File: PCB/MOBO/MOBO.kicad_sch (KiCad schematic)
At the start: 6 parts, among them J103 RPi_GPio, J104 RPi_GND, J105 RPi_5V, J106 RPi_DM, J107 RPi_DM, J7 RPi_TV

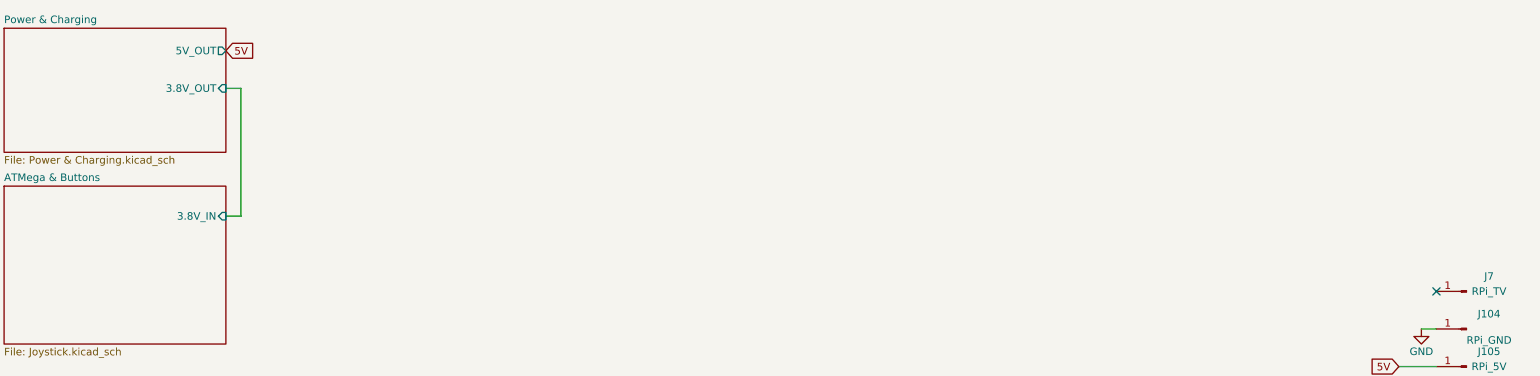
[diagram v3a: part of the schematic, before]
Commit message: fixed sheet conections and added wiring
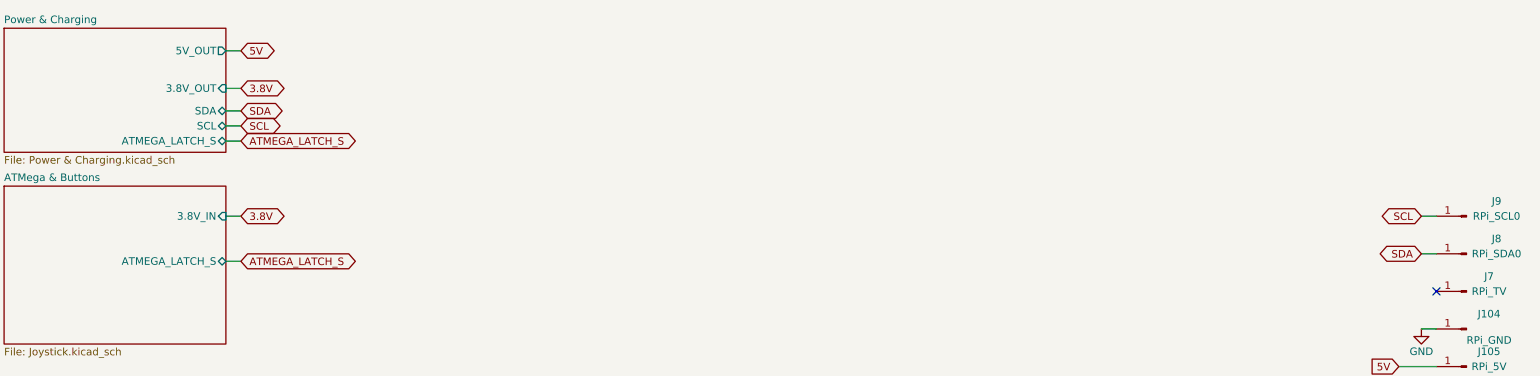
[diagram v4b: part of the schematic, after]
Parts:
- added J8: RPi_SDA0, TestPoint:TestPoint_Pad_1.5x1.5mm, symbol Connector:Conn_01x01_Male
- added J9: RPi_SCL0, TestPoint:TestPoint_Pad_1.5x1.5mm, symbol Connector:Conn_01x01_Male
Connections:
- new net SCL: J9.1 (Pin_1)
- new net SDA: J8.1 (Pin_1)
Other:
- sheet ATMega & Buttons ports: added ATMEGA_LATCH_S; removed none
- sheet Power & Charging ports: added ATMEGA_LATCH_S, SCL, SDA; removed none
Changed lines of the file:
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@@
   (no_connect (at 273.05 148.59))
   (no_connect (at 273.05 102.87))
+  (wire (pts (xy 264.16 57.15) (xy 261.62 57.15))
+    (stroke (width 0) (type default))
+  )
   (wire (pts (xy 59.69 29.21) (xy 62.23 29.21))
     (stroke (width 0) (type default))
   )
-  (wire (pts (xy 62.23 50.8) (xy 59.69 50.8))
+  (wire (pts (xy 59.69 35.56) (xy 62.23 35.56))
+    (stroke (width 0) (type default))
+  )
+  (wire (pts (xy 264.16 50.8) (xy 261.62 50.8))
     (stroke (width 0) (type default))
   )
@@
     (stroke (width 0) (type default))
   )
-  (wire (pts (xy 62.23 29.21) (xy 62.23 50.8))
+  (wire (pts (xy 59.69 58.42) (xy 62.23 58.42))
+    (stroke (width 0) (type default))
+  )
+  (wire (pts (xy 59.69 38.1) (xy 62.23 38.1))
+    (stroke (width 0) (type default))
+  )
+  (wire (pts (xy 59.69 22.86) (xy 62.23 22.86))
+    (stroke (width 0) (type default))
+  )
+  (wire (pts (xy 59.69 50.8) (xy 62.23 50.8))
     (stroke (width 0) (type default))
   )
   (wire (pts (xy 257.81 76.2) (xy 264.16 76.2))
+    (stroke (width 0) (type default))
+  )
+  (wire (pts (xy 59.69 33.02) (xy 62.23 33.02))
     (stroke (width 0) (type default))
   )
@@
     (effects (font (size 1.27 1.27)) (justify left bottom))
   )
-  (global_label "5V" (shape input) (at 59.69 22.86 0) (fields_autoplaced)
-    (effects (font (size 1.27 1.27)) (justify left))
-    (property "Intersheetrefs" "${INTERSHEET_REFS}" (at 64.9733 22.86 0)
-      (effects (font (size 1.27 1.27)) (justify left) hide)
+  (global_label "ATMEGA_LATCH_S" (shape bidirectional) (at 62.23 38.1 0) (fields_autoplaced)
+    (effects (font (size 1.27 1.27)) (justify left))
+    (property "Intersheetrefs" "${INTERSHEET_REFS}" (at 82.1712 38.1 0)
+      (effects (font (size 1.27 1.27)) (justify left) hide)
+    )
+  )
+  (global_label "ATMEGA_LATCH_S" (shape bidirectional) (at 62.23 58.42 0) (fields_autoplaced)
+    (effects (font (size 1.27 1.27)) (justify left))
+    (property "Intersheetrefs" "${INTERSHEET_REFS}" (at 82.1712 58.42 0)
+      (effects (font (size 1.27 1.27)) (justify left) hide)
+    )
+  )
+  (global_label "SCL" (shape bidirectional) (at 261.62 50.8 180) (fields_autoplaced)
+    (effects (font (size 1.27 1.27)) (justify right))
+    (property "Intersheetrefs" "${INTERSHEET_REFS}" (at 254.0159 50.8 0)
+      (effects (font (size 1.27 1.27)) (justify right) hide)
+    )
+  )
+  (global_label "5V" (shape bidirectional) (at 62.23 22.86 0) (fields_autoplaced)
+    (effects (font (size 1.27 1.27)) (justify left))
+    (property "Intersheetrefs" "${INTERSHEET_REFS}" (at 68.6246 22.86 0)
+      (effects (font (size 1.27 1.27)) (justify left) hide)
+    )
+  )
+  (global_label "SDA" (shape bidirectional) (at 261.62 57.15 180) (fields_autoplaced)
+    (effects (font (size 1.27 1.27)) (justify right))
+    (property "Intersheetrefs" "${INTERSHEET_REFS}" (at 253.9554 57.15 0)
+      (effects (font (size 1.27 1.27)) (justify right) hide)
     )
   )
@@
     (property "Intersheetrefs" "${INTERSHEET_REFS}" (at 252.5267 76.2 0)
       (effects (font (size 1.27 1.27)) (justify right) hide)
+    )
+  )
+  (global_label "SCL" (shape bidirectional) (at 62.23 35.56 0) (fields_autoplaced)
+    (effects (font (size 1.27 1.27)) (justify left))
+    (property "Intersheetrefs" "${INTERSHEET_REFS}" (at 69.8341 35.56 0)
+      (effects (font (size 1.27 1.27)) (justify left) hide)
+    )
+  )
+  (global_label "3.8V" (shape bidirectional) (at 62.23 50.8 0) (fields_autoplaced)
+    (effects (font (size 1.27 1.27)) (justify left))
+    (property "Intersheetrefs" "${INTERSHEET_REFS}" (at 70.4389 50.8 0)
+      (effects (font (size 1.27 1.27)) (justify left) hide)
+    )
+  )
+  (global_label "3.8V" (shape bidirectional) (at 62.23 29.21 0) (fields_autoplaced)
+    (effects (font (size 1.27 1.27)) (justify left))
+    (property "Intersheetrefs" "${INTERSHEET_REFS}" (at 70.4389 29.21 0)
+      (effects (font (size 1.27 1.27)) (justify left) hide)
+    )
+  )
+  (global_label "SDA" (shape bidirectional) (at 62.23 33.02 0) (fields_autoplaced)
+    (effects (font (size 1.27 1.27)) (justify left))
+    (property "Intersheetrefs" "${INTERSHEET_REFS}" (at 69.8946 33.02 0)
+      (effects (font (size 1.27 1.27)) (justify left) hide)
+    )
+  )
+  (symbol (lib_id "Connector:Conn_01x01_Male") (at 269.24 50.8 180) (unit 1)
+    (in_bom yes) (on_board yes) (dnp no)
+    (property "Reference" "J9" (at 274.32 48.26 0)
+      (effects (font (size 1.27 1.27)))
+    )
+    (property "Value" "RPi_SCL0" (at 274.32 50.8 0)
+      (effects (font (size 1.27 1.27)))
+    )
+    (property "Footprint" "TestPoint:TestPoint_Pad_1.5x1.5mm" (at 269.24 50.8 0)
+      (effects (font (size 1.27 1.27)) hide)
+    )
+    (property "Datasheet" "~" (at 269.24 50.8 0)
+      (effects (font (size 1.27 1.27)) hide)
+    )
+    (pin "1")
+    (instances
+      (project "MOBO"
+        (path "/2d62a3c1-c4f2-4921-9f6b-8dc8aef69d64"
+          (reference "J9") (unit 1)
+        )
+      )
     )
   )
@@
     )
   )
+  (symbol (lib_id "Connector:Conn_01x01_Male") (at 269.24 57.15 180) (unit 1)
+    (in_bom yes) (on_board yes) (dnp no)
+    (property "Reference" "J8" (at 274.32 54.61 0)
+      (effects (font (size 1.27 1.27)))
+    )
+    (property "Value" "RPi_SDA0" (at 274.32 57.15 0)
+      (effects (font (size 1.27 1.27)))
+    )
+    (property "Footprint" "TestPoint:TestPoint_Pad_1.5x1.5mm" (at 269.24 57.15 0)
+      (effects (font (size 1.27 1.27)) hide)
+    )
+    (property "Datasheet" "~" (at 269.24 57.15 0)
+      (effects (font (size 1.27 1.27)) hide)
+    )
+    (pin "1")
+    (instances
+      (project "MOBO"
+        (path "/2d62a3c1-c4f2-4921-9f6b-8dc8aef69d64"
+          (reference "J8") (unit 1)
+        )
+      )
+    )
+  )
   (symbol (lib_id "power:GND") (at 261.62 69.85 0) (unit 1)
     (in_bom yes) (on_board yes) (dnp no)
@@
       (effects (font (size 1.27 1.27)) (justify right))
     )
+    (pin "ATMEGA_LATCH_S" bidirectional (at 59.69 58.42 0)
+      (effects (font (size 1.27 1.27)) (justify right))
+    )
     (instances
       (project "MOBO"
@@
       (effects (font (size 1.27 1.27)) (justify right))
     )
+    (pin "SDA" bidirectional (at 59.69 33.02 0)
+      (effects (font (size 1.27 1.27)) (justify right))
+    )
+    (pin "SCL" bidirectional (at 59.69 35.56 0)
+      (effects (font (size 1.27 1.27)) (justify right))
+    )
+    (pin "ATMEGA_LATCH_S" bidirectional (at 59.69 38.1 0)
+      (effects (font (size 1.27 1.27)) (justify right))
+    )

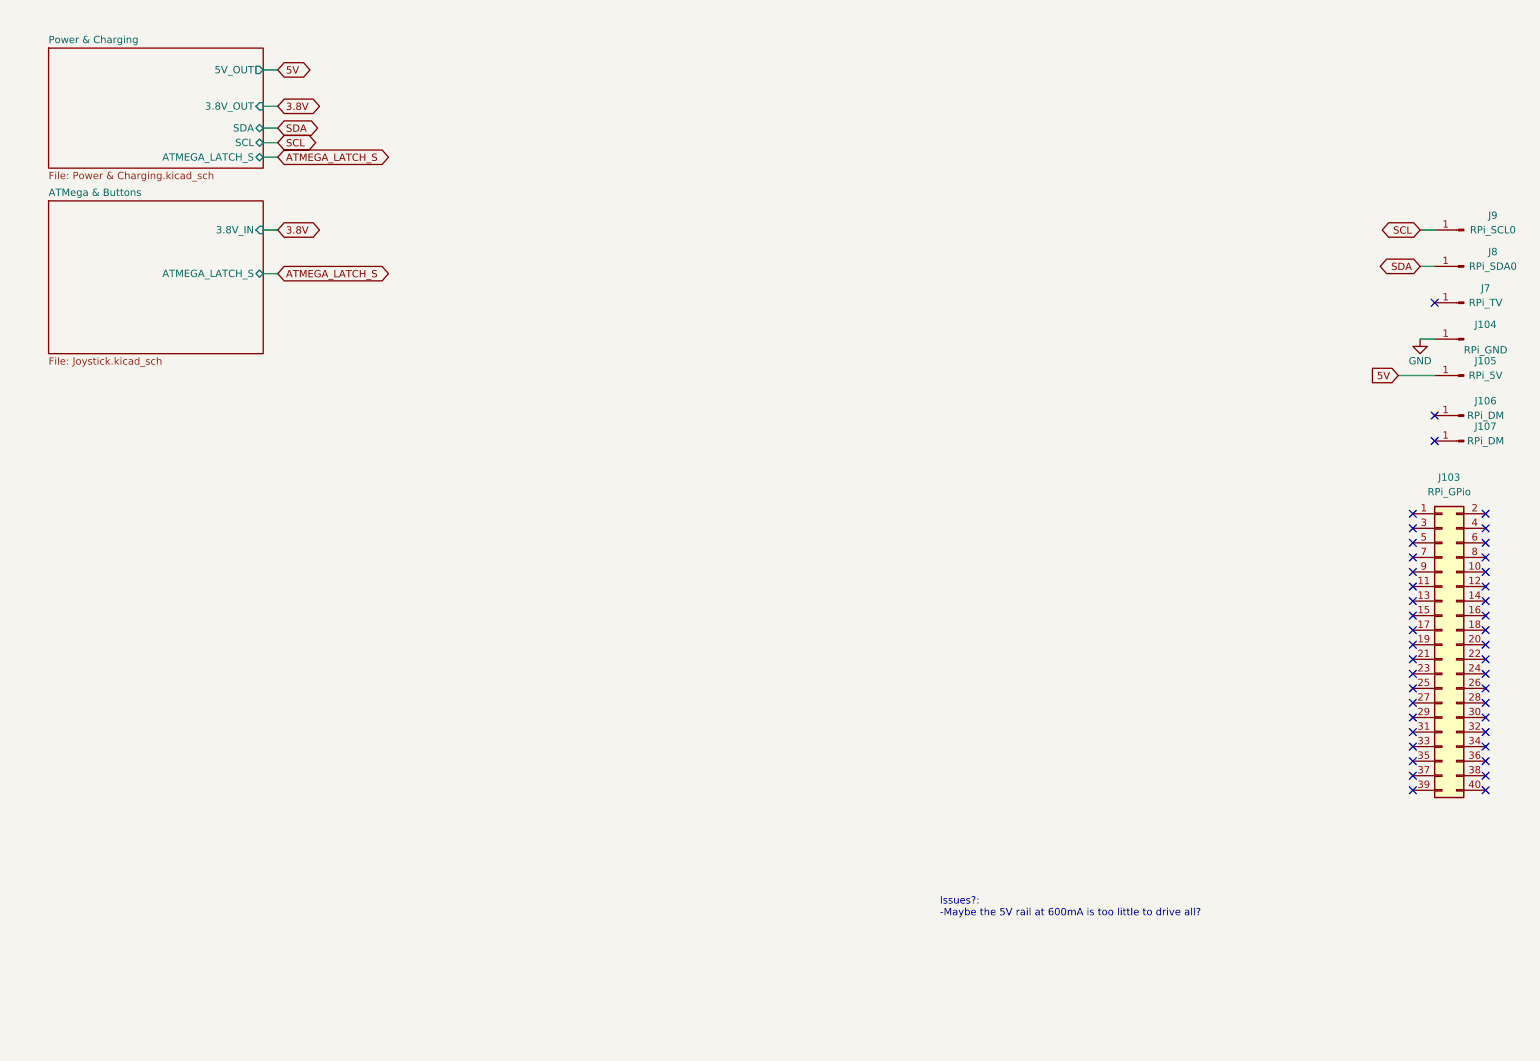
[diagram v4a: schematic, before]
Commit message: added 5V-GND-TV lines
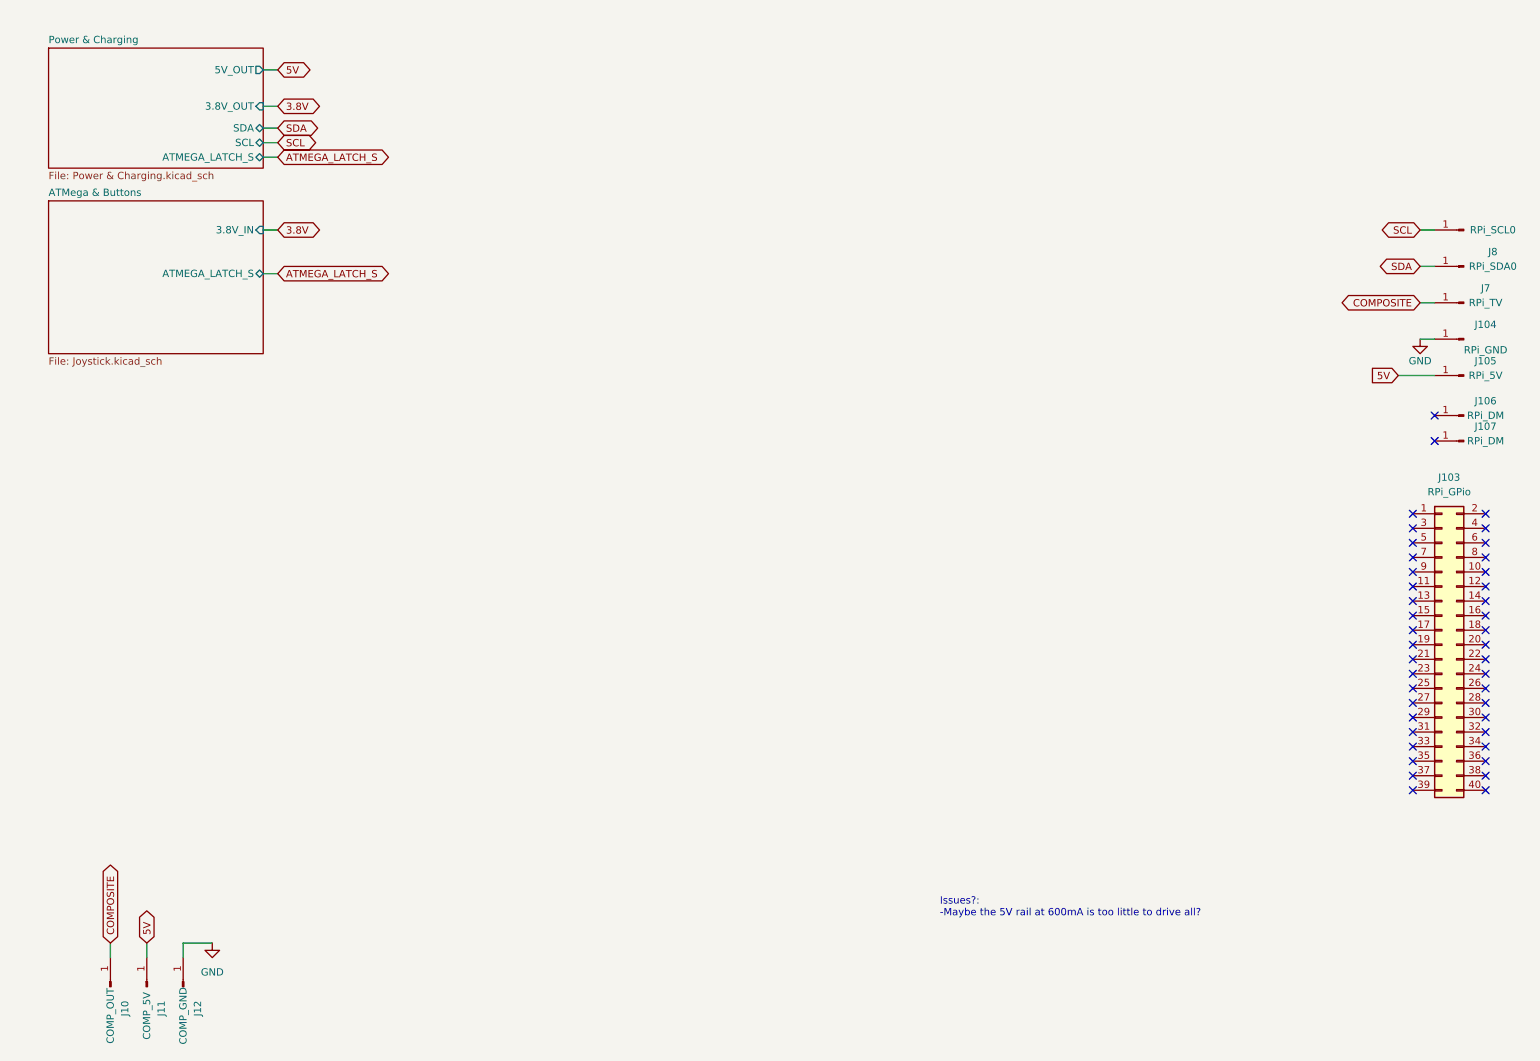
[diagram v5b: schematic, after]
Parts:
- added J10: COMP_OUT, TestPoint:TestPoint_Pad_1.5x1.5mm, symbol Connector:Conn_01x01_Male
- added J11: COMP_5V, TestPoint:TestPoint_Pad_1.5x1.5mm, symbol Connector:Conn_01x01_Male
- added J12: COMP_GND, TestPoint:TestPoint_Pad_1.5x1.5mm, symbol Connector:Conn_01x01_Male
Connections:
- net 5V: now also J11.1 (Pin_1)
- net GND: now also J12.1 (Pin_1)
- net COMPOSITE: now reaches J7.1 (Pin_1)
- net COMPOSITE: now also J10.1 (Pin_1)
- no-connect marks 43 -> 42
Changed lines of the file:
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@@
   (no_connect (at 273.05 120.65))
   (no_connect (at 260.35 102.87))
-  (no_connect (at 264.16 63.5))
   (no_connect (at 273.05 140.97))
   (no_connect (at 260.35 115.57))
@@
     (stroke (width 0) (type default))
   )
+  (wire (pts (xy 33.02 175.26) (xy 33.02 177.8))
+    (stroke (width 0) (type default))
+  )
   (wire (pts (xy 261.62 69.85) (xy 264.16 69.85))
     (stroke (width 0) (type default))
@@
     (stroke (width 0) (type default))
   )
+  (wire (pts (xy 45.72 175.26) (xy 50.8 175.26))
+    (stroke (width 0) (type default))
+  )
+  (wire (pts (xy 39.37 175.26) (xy 39.37 177.8))
+    (stroke (width 0) (type default))
+  )
   (wire (pts (xy 59.69 22.86) (xy 62.23 22.86))
+    (stroke (width 0) (type default))
+  )
+  (wire (pts (xy 45.72 175.26) (xy 45.72 177.8))
+    (stroke (width 0) (type default))
+  )
+  (wire (pts (xy 261.62 63.5) (xy 264.16 63.5))
     (stroke (width 0) (type default))
   )
@@
     )
   )
+  (global_label "COMPOSITE" (shape bidirectional) (at 33.02 175.26 90) (fields_autoplaced)
+    (effects (font (size 1.27 1.27)) (justify left))
+    (property "Intersheetrefs" "${INTERSHEET_REFS}" (at 33.02 160.5802 90)
+      (effects (font (size 1.27 1.27)) (justify left) hide)
+    )
+  )
+  (global_label "5V" (shape bidirectional) (at 39.37 175.26 90) (fields_autoplaced)
+    (effects (font (size 1.27 1.27)) (justify left))
+    (property "Intersheetrefs" "${INTERSHEET_REFS}" (at 39.37 168.8654 90)
+      (effects (font (size 1.27 1.27)) (justify left) hide)
+    )
+  )
   (global_label "5V" (shape input) (at 257.81 76.2 180) (fields_autoplaced)
     (effects (font (size 1.27 1.27)) (justify right))
@@
     )
   )
+  (global_label "COMPOSITE" (shape bidirectional) (at 261.62 63.5 180) (fields_autoplaced)
+    (effects (font (size 1.27 1.27)) (justify right))
+    (property "Intersheetrefs" "${INTERSHEET_REFS}" (at 246.9402 63.5 0)
+      (effects (font (size 1.27 1.27)) (justify right) hide)
+    )
+  )
+  (symbol (lib_id "Connector:Conn_01x01_Male") (at 45.72 182.88 90) (unit 1)
+    (in_bom yes) (on_board yes) (dnp no)
+    (property "Reference" "J12" (at 48.26 186.69 0)
+      (effects (font (size 1.27 1.27)))
+    )
+    (property "Value" "COMP_GND" (at 45.72 187.96 0)
+      (effects (font (size 1.27 1.27)))
+    )
+    (property "Footprint" "TestPoint:TestPoint_Pad_1.5x1.5mm" (at 45.72 182.88 0)
+      (effects (font (size 1.27 1.27)) hide)
+    )
+    (property "Datasheet" "~" (at 45.72 182.88 0)
+      (effects (font (size 1.27 1.27)) hide)
+    )
+    (pin "1")
+    (instances
+      (project "MOBO"
+        (path "/2d62a3c1-c4f2-4921-9f6b-8dc8aef69d64"
+          (reference "J12") (unit 1)
+        )
+      )
+    )
+  )
   (symbol (lib_id "Connector:Conn_01x01_Male") (at 269.24 50.8 180) (unit 1)
     (in_bom yes) (on_board yes) (dnp no)
     (property "Reference" "J9" (at 274.32 48.26 0)
-      (effects (font (size 1.27 1.27)))
+      (effects (font (size 1.27 1.27)) hide)
     )
     (property "Value" "RPi_SCL0" (at 274.32 50.8 0)
@@
     )
   )
+  (symbol (lib_id "Connector:Conn_01x01_Male") (at 39.37 182.88 90) (unit 1)
+    (in_bom yes) (on_board yes) (dnp no)
+    (property "Reference" "J11" (at 41.91 186.69 0)
+      (effects (font (size 1.27 1.27)))
+    )
+    (property "Value" "COMP_5V" (at 39.37 187.96 0)
+      (effects (font (size 1.27 1.27)))
+    )
+    (property "Footprint" "TestPoint:TestPoint_Pad_1.5x1.5mm" (at 39.37 182.88 0)
+      (effects (font (size 1.27 1.27)) hide)
+    )
+    (property "Datasheet" "~" (at 39.37 182.88 0)
+      (effects (font (size 1.27 1.27)) hide)
+    )
+    (pin "1")
+    (instances
+      (project "MOBO"
+        (path "/2d62a3c1-c4f2-4921-9f6b-8dc8aef69d64"
+          (reference "J11") (unit 1)
+        )
+      )
+    )
+  )
   (symbol (lib_id "power:GND") (at 261.62 69.85 0) (unit 1)
     (in_bom yes) (on_board yes) (dnp no)
@@
         )
       )
+    )
+  )
+  (symbol (lib_id "power:GND") (at 50.8 175.26 0) (unit 1)
+    (in_bom yes) (on_board yes) (dnp no) (fields_autoplaced)
+    (property "Reference" "#PWR028" (at 50.8 181.61 0)
+      (effects (font (size 1.27 1.27)) hide)
+    )
+    (property "Value" "GND" (at 50.8 180.34 0)
+      (effects (font (size 1.27 1.27)))
+    )
+    (property "Footprint" "" (at 50.8 175.26 0)
+      (effects (font (size 1.27 1.27)) hide)
+    )
+    (property "Datasheet" "" (at 50.8 175.26 0)
+      (effects (font (size 1.27 1.27)) hide)
+    )
+    (pin "1")
+    (instances
+      (project "MOBO"
+        (path "/2d62a3c1-c4f2-4921-9f6b-8dc8aef69d64"
+          (reference "#PWR028") (unit 1)
+        )
+      )
+    )
+  )
+  (symbol (lib_id "Connector:Conn_01x01_Male") (at 33.02 182.88 90) (unit 1)
+    (in_bom yes) (on_board yes) (dnp no)
+    (property "Reference" "J10" (at 35.56 186.69 0)
+      (effects (font (size 1.27 1.27)))
+    )
+    (property "Value" "COMP_OUT" (at 33.02 187.96 0)
+      (effects (font (size 1.27 1.27)))
+    )
+    (property "Footprint" "TestPoint:TestPoint_Pad_1.5x1.5mm" (at 33.02 182.88 0)
+      (effects (font (size 1.27 1.27)) hide)
+    )
+    (property "Datasheet" "~" (at 33.02 182.88 0)
+      (effects (font (size 1.27 1.27)) hide)
+    )
+    (pin "1")
+    (instances
+      (project "MOBO"
+        (path "/2d62a3c1-c4f2-4921-9f6b-8dc8aef69d64"
+          (reference "J10") (unit 1)
+        )
+      )
